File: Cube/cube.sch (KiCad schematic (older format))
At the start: 14 parts

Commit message: Added humidity/gyro sensors to the cube pcb
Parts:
- added C? (x2): 10uF, symbol Device:C
- added C? (x2): 100nF, symbol Device:C
- added PullUp: 10k, symbol Device:R_Small
- added U?: L3GD20H, LGA-16_3X3X1_STM, symbol gyro:L3GD20H
- added U?: Si7007-A20, symbol Sensor_Humidity_New:7007
- U?: symbol zigbee:AT86RF231-ZU -> cube-rescue:AT86RF231-ZU-zigbee
- U?: symbol pic18f47:PIC18F47K40-I_P -> cube-rescue:PIC18F47K40-I_P-pic18f47
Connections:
- net labels added: +1V8, DRDY_INT2, INT1, RHOut, SPI_CS2, TempOut
- wire segments 85 -> 133

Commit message: Edit cube pcb style
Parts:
- U?: symbol gyro:L3GD20H -> cube-rescue:L3GD20H-gyro
- U?: symbol Sensor_Humidity_New:7007 -> cube-rescue:7007-Sensor_Humidity_New
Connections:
- net labels added: RH_OUT, TEMP_OUT
- net labels removed: RHOut, TempOut
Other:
- moved on the sheet: CX?, PullUp, XTAL?

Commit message: Finish LED scematics
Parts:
- added J?: Conn_01x03_Male, symbol Connector:Conn_01x03_Male
- gave numbers to parts that had none: 2
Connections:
- net GND: now also J?.1 (Pin_1)
- net LED_DATA: now reaches U?.2 (RA0)
- net LED_DATA: now also J?.2 (Pin_2)
- new net +5V: J?.3 (Pin_3)

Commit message: Update
Zigbee update:
- Added custom made symbol: SMD Balun - 2450FB15L0001E
- Added Antenna - Ceramic chip: W3043

Note: There might be a missing capacitor in the communication between the antenna to the Balun - some circuit reference does have it some doesn't
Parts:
- added B?: 2450FB15L0001E, symbol Balun:2450FB15L0001E
- added C1, C2, C3: 22pF, symbol Device:C_Small
- added W3043: 2.4GHz, symbol Device:Antenna
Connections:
- wire segments 137 -> 154
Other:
- moved on the sheet: CX, XTAL

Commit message: Add motor to the cube schematics
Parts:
- added 1k: R, symbol Device:R
- added C: 0.1uF, symbol pspice:C
- added D?: DIODE, symbol pspice:DIODE
- added Motor: C0720B001F, XDCR_C0720B001F, symbol C0720B001F:C0720B001F
- added Q1: 2N2219, Package_TO_SOT_THT:TO-39-3, symbol Transistor_BJT:2N2219
- B?: symbol Balun:2450FB15L0001E -> cube-rescue:2450FB15L0001E-Balun
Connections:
- net labels added: MOTOR_OUT
- wire segments 154 -> 169
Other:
- note added: "CUBE MCU"
- note added: "HUMID/TEMP SENSOR"
- note added: "LED CONNECTORS"
- note added: "MEMS MOTION SENSOR"
- note added: "POWER SUPPLY"
- note added: "VIBRATION MOTOR"
- note added: "ZIGBEE TRANC"
- moved on the sheet: C1, C2, C3, CX, PullUp, W3043, XTAL

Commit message: fixed power circuit
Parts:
- added C1: 10uF, symbol Device:C
- added C2, C3: 100nF, symbol Device:C
- added C?: C, symbol Device:C
- added L1: 5.6uH, symbol Device:L
- added R?: 30Ω, symbol Device:R
- added R?: 10kΩ, symbol Device:R
- added R?: 52.3kΩ, symbol Device:R
- added U?: TPS56339DDC, Package_TO_SOT_SMD:SOT-23-6, symbol Regulator_Switching:TPS56339DDC
- Motor: symbol C0720B001F:C0720B001F -> cube-rescue:C0720B001F-C0720B001F
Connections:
- net +5V: now also C3.1, C?.1, L1.1, U?.2 (SW)
- new net: C1.2, C2.2, C?.2, R?.2, U?.1 (GND)
- new net: C3.2, R?.1
- new net: R?.2, U?.6 (BOOT)
- new net: R?.1, R?.2, U?.4 (FB)
- new net: L1.2, R?.1
- new net VCC: C1.1, C2.1, U?.3 (VIN)
- no-connect marks 1 -> 2
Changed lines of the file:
@@
 LED CONNECTORS
 $Comp
-L C0720B001F:C0720B001F Motor
+L cube-rescue:C0720B001F-C0720B001F Motor
 U 1 1 608DBFBC
 P 15200 7700
@@
 Wire Wire Line
 	1750 1700 1400 1700
+$Comp
+L power:VCC #PWR?
+U 1 1 607F567C
+P 2650 7950
+F 0 "#PWR?" H 2650 7800 50  0001 C CNN
+F 1 "VCC" H 2665 8123 50  0000 C CNN
+F 2 "" H 2650 7950 50  0001 C CNN
+F 3 "" H 2650 7950 50  0001 C CNN
+	1    2650 7950
+	1    0    0    -1
+$EndComp
+$Comp
+L Device:C C1
+U 1 1 607F68EB
+P 2750 8600
+F 0 "C1" H 2865 8646 50  0000 L CNN
+F 1 "10uF" H 2865 8555 50  0000 L CNN
+F 2 "" H 2788 8450 50  0001 C CNN
+F 3 "~" H 2750 8600 50  0001 C CNN
+	1    2750 8600
+	1    0    0    -1
+$EndComp
+$Comp
+L Device:C C2
+U 1 1 607F7E0F
+P 3200 8600
+F 0 "C2" H 3315 8646 50  0000 L CNN
+F 1 "100nF" H 3315 8555 50  0000 L CNN
+F 2 "" H 3238 8450 50  0001 C CNN
+F 3 "~" H 3200 8600 50  0001 C CNN
+	1    3200 8600
+	1    0    0    -1
+$EndComp
+$Comp
+L Device:C C3
+U 1 1 608001FD
+P 4750 7750
+F 0 "C3" H 4865 7796 50  0000 L CNN
+F 1 "100nF" H 4865 7705 50  0000 L CNN
+F 2 "" H 4788 7600 50  0001 C CNN
+F 3 "~" H 4750 7750 50  0001 C CNN
+	1    4750 7750
+	1    0    0    -1
+$EndComp
+$Comp
+L Device:C C?
+U 1 1 6080829B
+P 5550 8250
+F 0 "C?" H 5665 8296 50  0000 L CNN
+F 1 "C" H 5665 8205 50  0000 L CNN
+F 2 "" H 5588 8100 50  0001 C CNN
+F 3 "~" H 5550 8250 50  0001 C CNN
+	1    5550 8250
+	1    0    0    -1
+$EndComp
+$Comp
+L Device:R R?
+U 1 1 6080FD37
+P 4750 8150
+F 0 "R?" H 4820 8196 50  0000 L CNN
+F 1 "30Ω" H 4820 8105 50  0000 L CNN
+F 2 "" V 4680 8150 50  0001 C CNN
+F 3 "~" H 4750 8150 50  0001 C CNN
+	1    4750 8150
+	1    0    0    -1
+$EndComp
+$Comp
+L Device:R R?
+U 1 1 60812A94
+P 5100 8700
+F 0 "R?" H 5170 8746 50  0000 L CNN
+F 1 "10kΩ" H 5170 8655 50  0000 L CNN
+F 2 "" V 5030 8700 50  0001 C CNN
+F 3 "~" H 5100 8700 50  0001 C CNN
+	1    5100 8700
+	1    0    0    -1
+$EndComp
+$Comp
+L Device:R R?
+U 1 1 6081A729
+P 5100 8150
+F 0 "R?" H 5170 8196 50  0000 L CNN
+F 1 "52.3kΩ" H 5170 8105 50  0000 L CNN
+F 2 "" V 5030 8150 50  0001 C CNN
+F 3 "~" H 5100 8150 50  0001 C CNN
+	1    5100 8150
+	1    0    0    -1
+$EndComp
+$Comp
+L Device:L L1
+U 1 1 6082276B
+P 5100 7750
+F 0 "L1" H 5153 7796 50  0000 L CNN
+F 1 "5.6uH" H 5153 7705 50  0000 L CNN
+F 2 "" H 5100 7750 50  0001 C CNN
+F 3 "~" H 5100 7750 50  0001 C CNN
+	1    5100 7750
+	1    0    0    -1
+$EndComp
+$Comp
+L Regulator_Switching:TPS56339DDC U?
+U 1 1 60823E0D
+P 4050 8400
+F 0 "U?" H 4050 8767 50  0000 C CNN
+F 1 "TPS56339DDC" H 4050 8676 50  0000 C CNN
+F 2 "Package_TO_SOT_SMD:SOT-23-6" H 4100 8150 50  0001 L CNN
+F 3 "https://www.ti.com/lit/ds/symlink/tps56339.pdf" H 4050 8400 50  0001 C CNN
+	1    4050 8400
+	1    0    0    -1
+$EndComp
+Wire Wire Line
+	2650 7950 2650 8300
+Wire Wire Line
+	3200 8450 3200 8300
+Connection ~ 3200 8300
+Wire Wire Line
+	3200 8300 3650 8300
+Wire Wire Line
+	4450 8400 4750 8400
+Wire Wire Line
+	4750 8400 4750 8300
+Wire Wire Line
+	4750 8000 4750 7900
+Wire Wire Line
+	5100 7900 5100 8000
+Wire Wire Line
+	5100 8300 5100 8500
+Wire Wire Line
+	5100 8500 5100 8550
+Connection ~ 5100 8500
+Wire Wire Line
+	5100 8850 5100 8900
+Wire Wire Line
+	4050 8900 4050 8700
+Wire Wire Line
+	3200 8750 3200 8900
+Connection ~ 3200 8900
+Wire Wire Line
+	3200 8900 4050 8900
+NoConn ~ 3650 8500
+Wire Wire Line
+	4450 8300 4600 8300
+Wire Wire Line
+	4600 8300 4600 7550
+Wire Wire Line
+	4600 7550 4750 7550
+Wire Wire Line
+	5550 7550 5550 8100
+Wire Wire Line
+	5550 8400 5550 8900
+Wire Wire Line
+	5100 7550 5100 7600
+Connection ~ 5100 7550
+Wire Wire Line
+	4750 7600 4750 7550
+$Comp
+L power:+5V #PWR?
+U 1 1 60966E96
+P 5950 7500
+F 0 "#PWR?" H 5950 7350 50  0001 C CNN
+F 1 "+5V" H 5965 7673 50  0000 C CNN
+F 2 "" H 5950 7500 50  0001 C CNN
+F 3 "" H 5950 7500 50  0001 C CNN
+	1    5950 7500
+	1    0    0    -1
+$EndComp
+Wire Wire Line
+	5950 7550 5950 7500
+Wire Wire Line
+	2650 8300 2750 8300
+Wire Wire Line
+	2750 8900 2750 8750
+Wire Wire Line
+	2750 8900 3200 8900
+Wire Wire Line
+	2750 8450 2750 8300
+Connection ~ 2750 8300
+Wire Wire Line
+	2750 8300 3200 8300
+Wire Wire Line
+	4450 8500 5100 8500
+Wire Wire Line
+	4050 8900 5100 8900
+Connection ~ 4050 8900
+Wire Wire Line
+	4750 7550 5100 7550
+Connection ~ 4750 7550
+Connection ~ 5550 7550
+Wire Wire Line
+	5550 7550 5950 7550
+Wire Wire Line
+	5100 7550 5550 7550
+Wire Wire Line
+	5100 8900 5550 8900
+Connection ~ 5100 8900
 $EndSCHEMATC

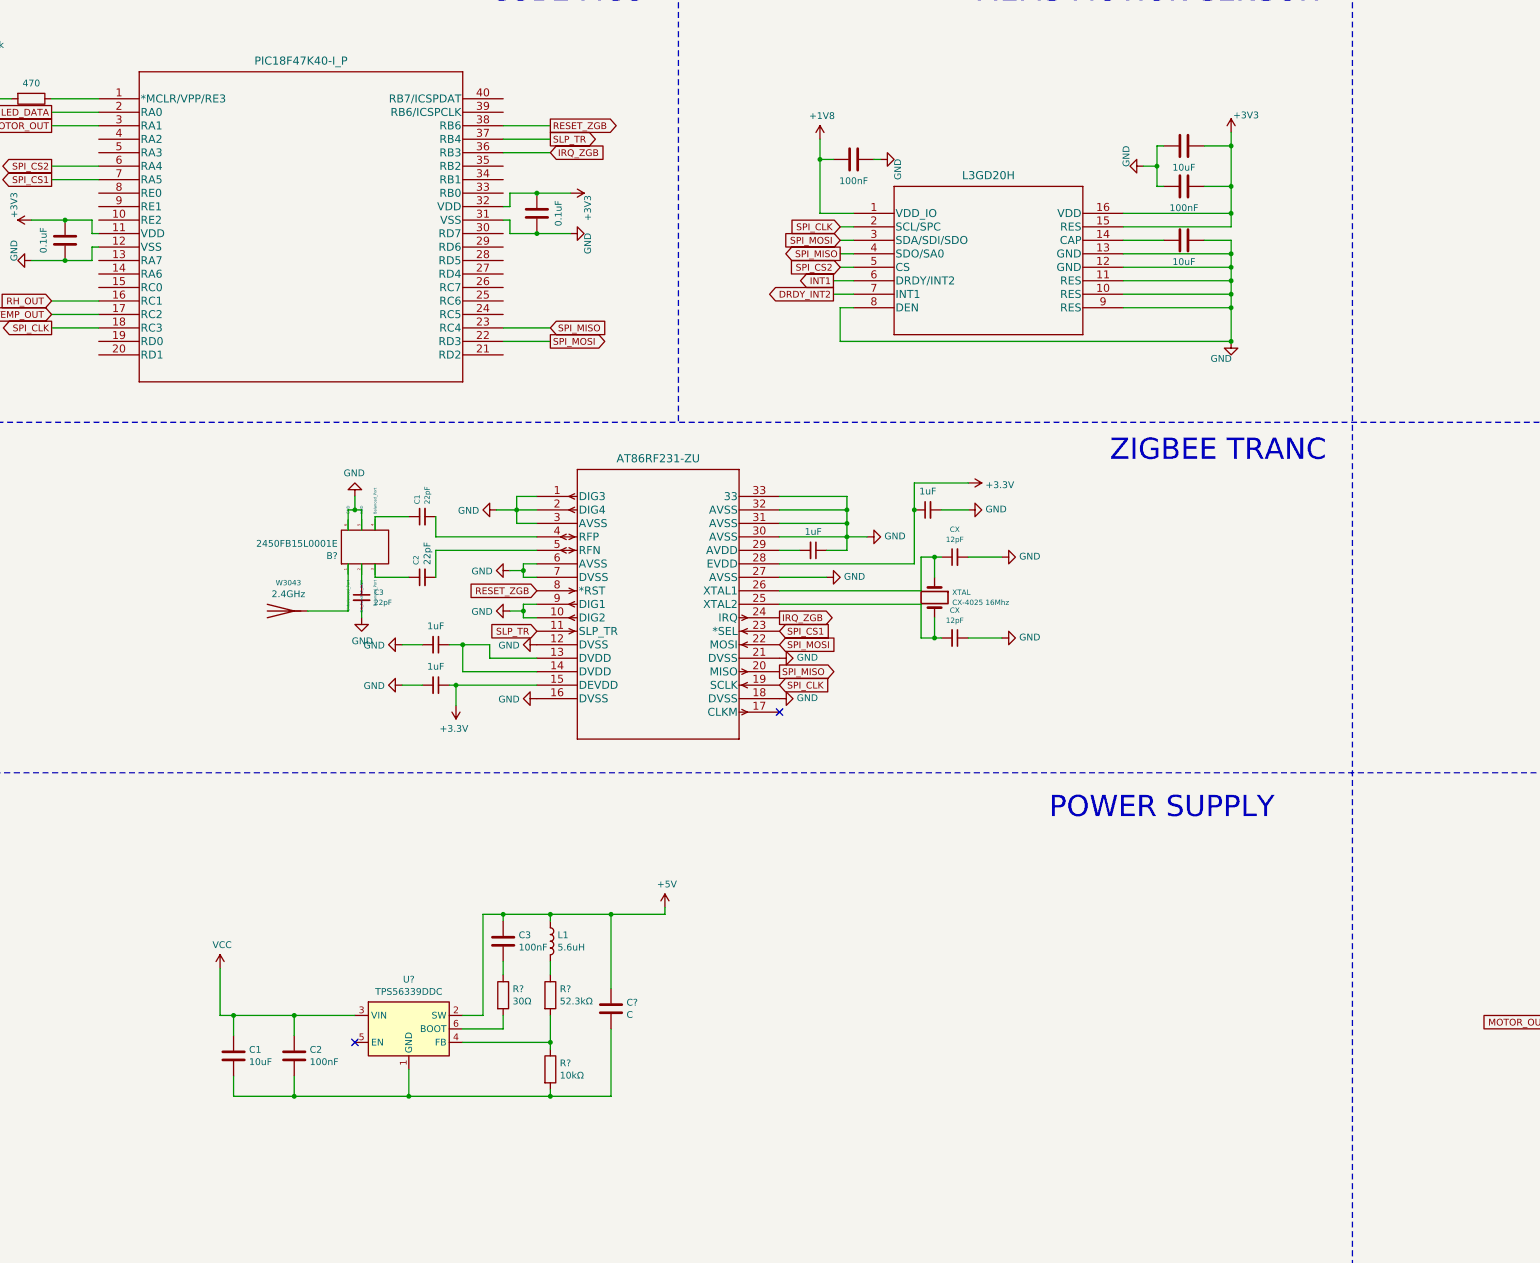
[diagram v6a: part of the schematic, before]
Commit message: Add power supply changes
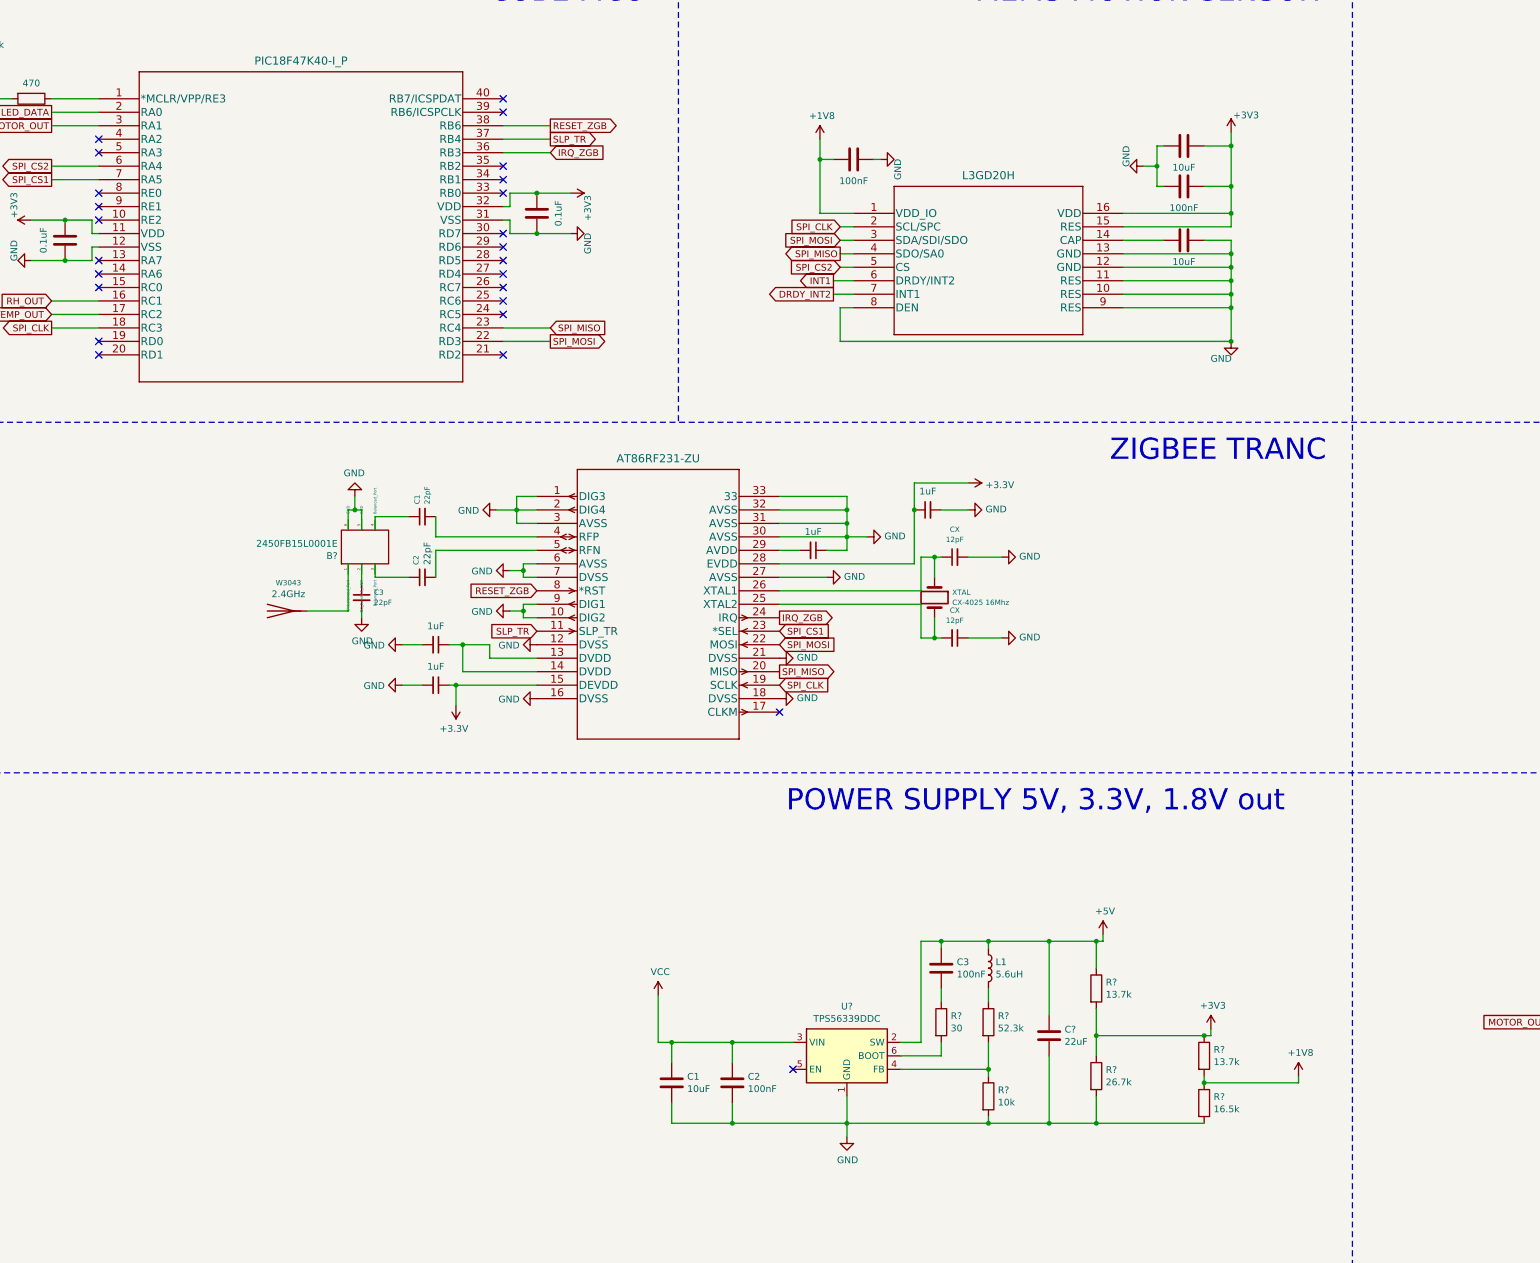
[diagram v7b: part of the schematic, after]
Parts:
- added R? (x2): 13.7k, symbol Device:R
- added R?: 26.7k, symbol Device:R
- added R?: 16.5k, symbol Device:R
- C?: value C -> 22uF
- R?: value 30Ω -> 30
- R?: value 10kΩ -> 10k
- R?: value 52.3kΩ -> 52.3k
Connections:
- net +1V8: now also R?.1, R?.2
- net +3V3: now also R?.1, R?.1, R?.2
- net +5V: now also R?.1
- net GND: now also C1.2, C2.2, C?.2, R?.2, U?.1 (GND), R?.2, R?.2
- no-connect marks 2 -> 25
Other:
- note added: "POWER SUPPLY 5V, 3.3V, 1.8V out"
- note removed: "POWER SUPPLY"
- moved on the sheet: C1, C2, C3, C?, L1, R?, U?

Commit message: Add programmable connectors
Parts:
- removed C?: 0.1uF, symbol Device:C
- removed R? (x2): 13.7k, symbol Device:R
- removed R?: 26.7k, symbol Device:R
- removed R?: 16.5k, symbol Device:R
- removed R?: 470, symbol Device:R
- removed R?: 10k, symbol Device:R
- added C? (x2): 10uF, symbol Device:C
- added C? (x4): 100nF, symbol Device:C
- added C? (x2): 22uF, symbol Device:C
- added J?: Conn_01x06_Male, symbol Connector:Conn_01x06_Male
- added L?: 4.7uH, symbol Device:L
- added L?: 2.2uH, symbol Device:L
- added R? (x2): 30, symbol Device:R
- added R? (x2): 10k, symbol Device:R
- added R?: 30.9k, symbol Device:R
- added R?: 12.4k, symbol Device:R
- added R?: 330, symbol Device:R
- added R?: 1k, symbol Device:R
- added U? (x2): TPS56339DDC, Package_TO_SOT_SMD:SOT-23-6, symbol Regulator_Switching:TPS56339DDC
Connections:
- net +1V8: now also C?.1, L?.2, R?.1
- net +3V3: now also C?.1, J?.2 (Pin_2), L?.2, R?.1, R?.1
- net +5V: now also L1.2, R?.1; no longer C3.1, L1.1, U?.2 (SW)
- net GND: now also C?.2, C?.2, C?.2, C?.2, C?.2, C?.2, J?.3 (Pin_3), R?.2, R?.2, U?.1 (GND), U?.1 (GND)
- net LED_DATA: now also R?.2; no longer J?.2 (Pin_2)
- net VCC: now also C?.1, C?.1, C?.1, C?.1, U?.3 (VIN), U?.3 (VIN)
- net MCLR: now reaches U?.1 (*MCLR/VPP/RE3)
- net MCLR: now also J?.1 (Pin_1), R?.2
- net PGC: now reaches U?.39 (RB6/ICSPCLK)
- net PGC: now also J?.5 (Pin_5)
- net PGD: now reaches U?.40 (RB7/ICSPDAT)
- net PGD: now also J?.4 (Pin_4)
- new net: J?.2 (Pin_2), R?.1
- new net: C3.1, L1.1, U?.2 (SW)
- new net: C?.1, L?.1, U?.2 (SW) (x2)
- new net: C?.2, R?.1 (x2)
- new net: R?.2, U?.6 (BOOT) (x2)
- new net: R?.1, R?.2, U?.4 (FB) (x2)
- no-connect marks 25 -> 26
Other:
- note added: "PICKIT CONNECTOR"
- moved on the sheet: C1, C2, C3, C?, L1, PullUp, R?, U?
